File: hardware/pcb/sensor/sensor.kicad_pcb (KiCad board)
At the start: 2 copper layers, 76.2 x 71.1 mm, 14 parts

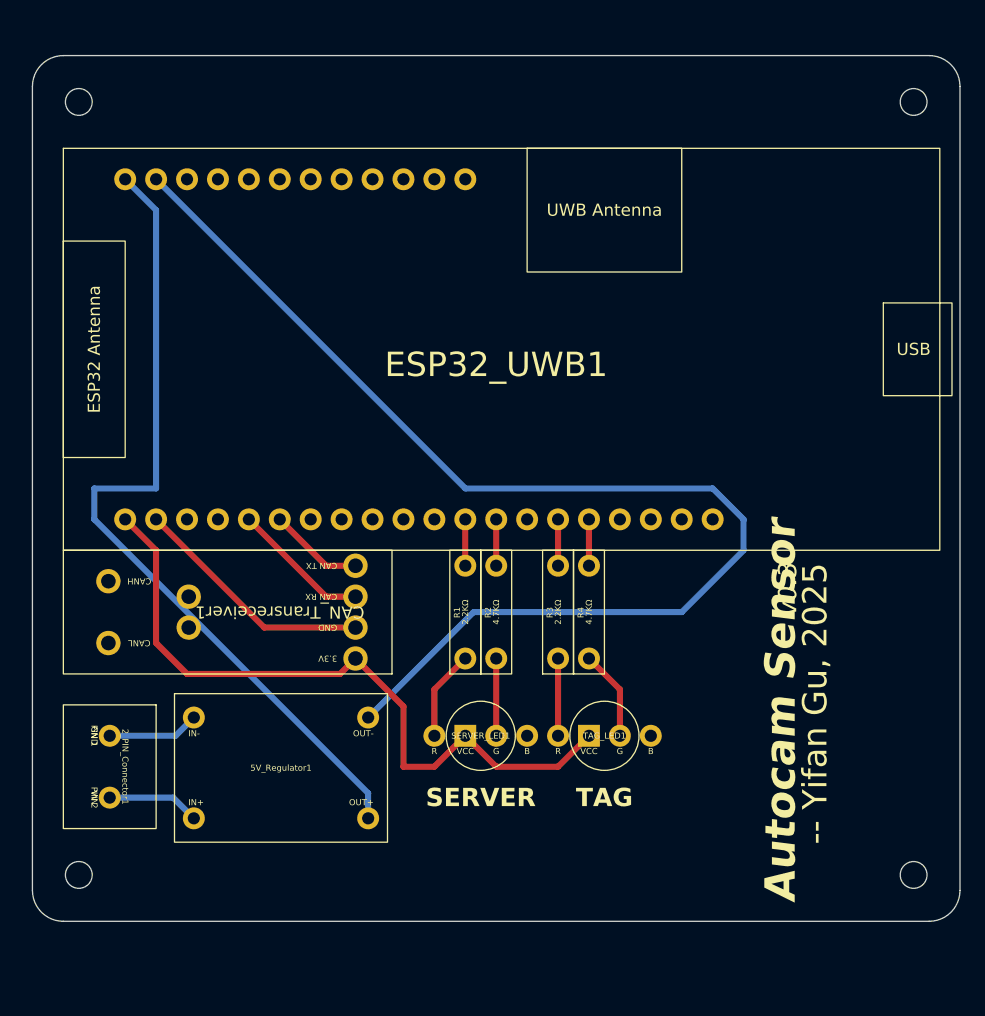
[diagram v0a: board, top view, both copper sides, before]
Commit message: remote: Update PCB for remote.
Fix the issue that GPIO 35 does not have internal PULLUP resistor.
So switch the pin with the gimbal thumbstick input Y, instead of the
drive mode button.

Update sensor and tag pcb as well to reflect the changes.
- tag: Use pin 39 for battery measurement and revert the resistor value
  change that's done in the previous commit.
- sensor: Fix a wiring issue.
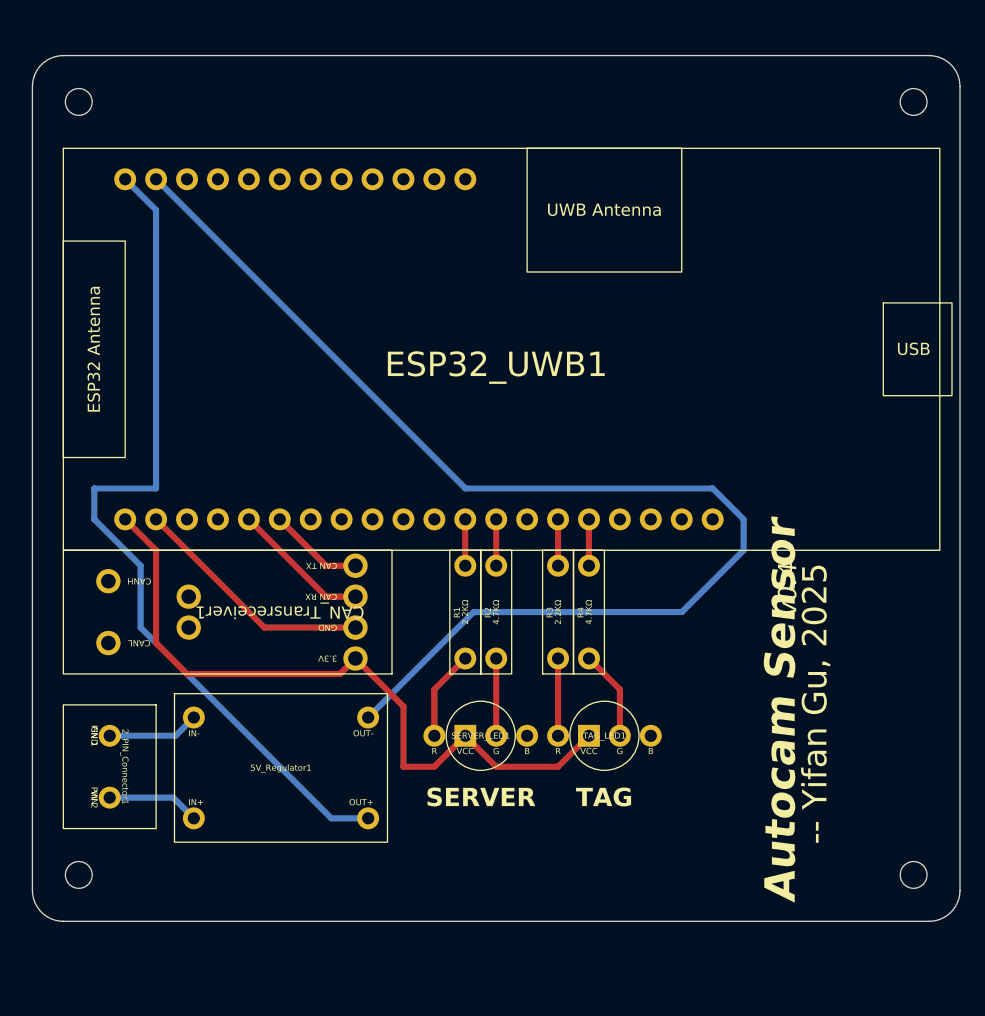
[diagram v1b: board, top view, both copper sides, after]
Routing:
- net Net-(5V_Regulator1-OUT+): track 68.0 -> 69.7 mm
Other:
- board text added: "v0.4"
- board text removed: "v0.3"
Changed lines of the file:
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@@
 	(title_block
 		(title "Autocam Sensor")
-		(date "2025-03-18")
-		(rev "v0.3")
+		(date "2025-03-27")
+		(rev "v0.4")
 	)
 	(layers
@@
 		)
 	)
-	(gr_text "v0.3"
+	(gr_text "v0.4"
 		(at 173.418978 111.513989 90)
 		(layer "F.SilkS")
@@
 			(justify right bottom)
 		)
-		(render_cache "v0.3" 90
+		(render_cache "v0.4" 90
 			(polygon
 				(pts
@@
 			(polygon
 				(pts
-					(xy 171.827481 111.538534) (xy 171.968165 111.691308) (xy 171.968165 112.155217) (xy 171.827481 112.285001)
+					(xy 172.415587 112.363312) (xy 171.849462 112.313669) (xy 171.997382 112.183793) (xy 172.379225 112.216308)
+					(xy 172.469076 112.313669)
 				)
 			)
 			(polygon
 				(pts
-					(xy 173.163978 111.655038) (xy 173.163978 112.401505) (xy 173.023294 112.246899) (xy 173.023294 111.782991)
-				)
-			)
-			(polygon
-				(pts
-					(xy 172.577795 111.576728) (xy 173.134668 111.62637) (xy 172.993893 111.754323) (xy 172.612141 111.721808)
+					(xy 172.577886 111.576728) (xy 173.141996 111.62637) (xy 172.993984 111.754323) (xy 172.612233 111.721808)
 					(xy 172.522565 111.624447)
 				)
@@
 			(polygon
 				(pts
-					(xy 172.379225 111.700833) (xy 171.997657 111.66841) (xy 171.854317 111.513713) (xy 172.415587 111.563355)
+					(xy 172.379225 111.700833) (xy 171.997657 111.66841) (xy 171.849462 111.513713) (xy 172.415587 111.563355)
 					(xy 172.469076 111.618768)
 				)
@@
 	)
 	(segment
-		(start 120.65 82.55)
-		(end 118.11 80.01)
+		(start 119.38 116.84)
+		(end 135.05 132.51)
 		(width 0.5)
 		(layer "B.Cu")
@@
 	)
 	(segment
-		(start 138.07 130.45)
+		(start 115.57 105.41)
 		(end 115.57 107.95)
 		(width 0.5)
@@
 	)
 	(segment
-		(start 120.65 105.41)
-		(end 120.65 82.55)
+		(start 120.65 82.55)
+		(end 120.65 105.41)
 		(width 0.5)
 		(layer "B.Cu")
@@
 	)
 	(segment
-		(start 138.07 132.51)
-		(end 138.07 130.45)
+		(start 118.11 80.01)
+		(end 120.65 82.55)
 		(width 0.5)
 		(layer "B.Cu")
@@
 	)
 	(segment
-		(start 115.57 105.41)
-		(end 120.65 105.41)
+		(start 119.38 111.76)
+		(end 119.38 116.84)
 		(width 0.5)
 		(layer "B.Cu")
@@
 	(segment
 		(start 115.57 107.95)
+		(end 119.38 111.76)
+		(width 0.5)
+		(layer "B.Cu")
+		(net 2)
+	)
+	(segment
+		(start 135.05 132.51)
+		(end 138.07 132.51)
+		(width 0.5)
+		(layer "B.Cu")
+		(net 2)
+	)
+	(segment
+		(start 120.65 105.41)
 		(end 115.57 105.41)
 		(width 0.5)

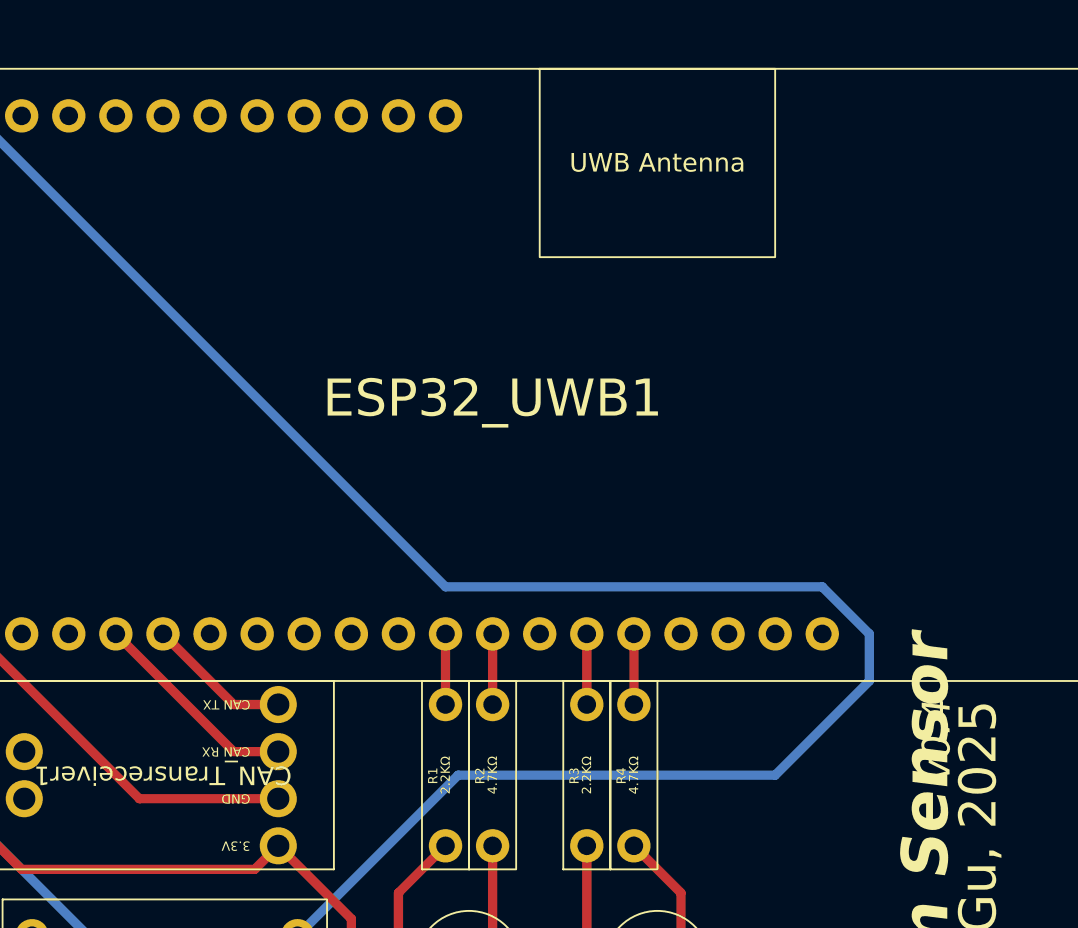
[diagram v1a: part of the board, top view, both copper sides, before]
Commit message: sensor,tag: Update PCB wiring to avoid bootstrap pins.
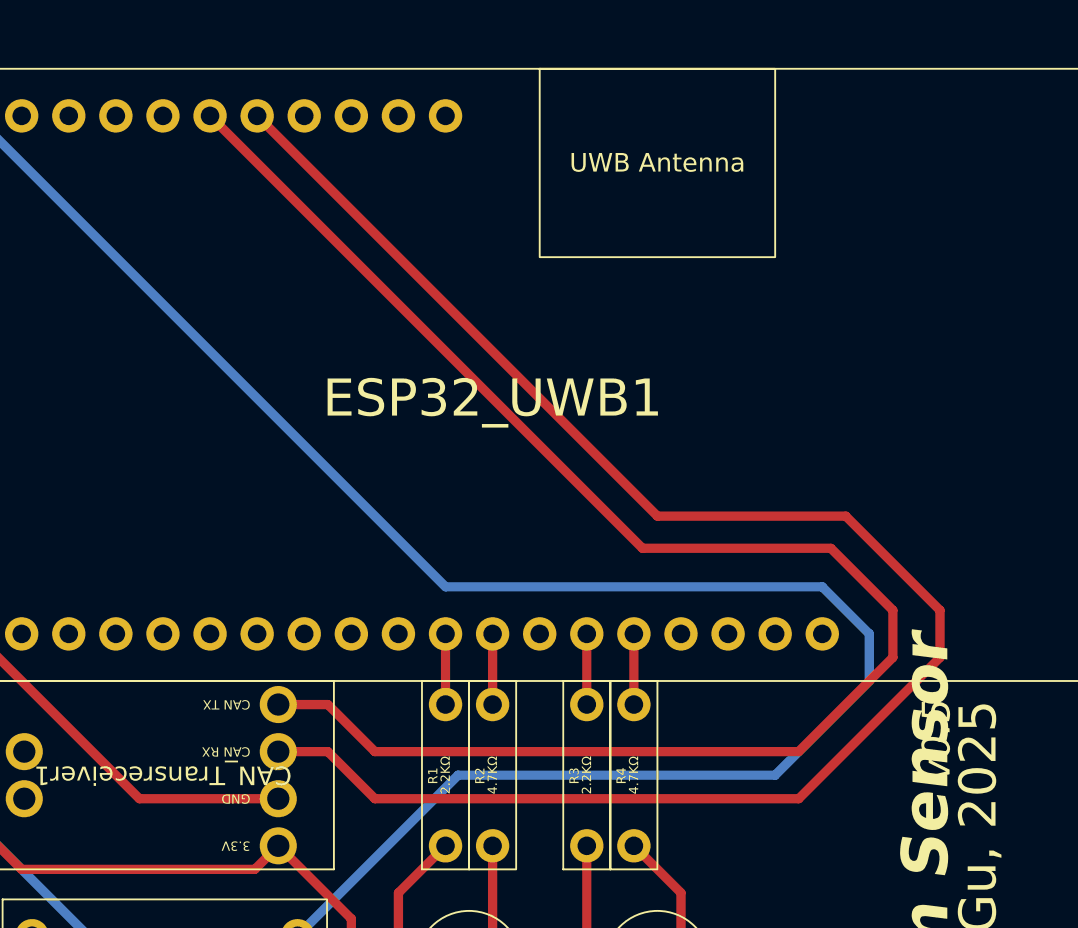
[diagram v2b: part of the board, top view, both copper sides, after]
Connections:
- ESP32_UWB1 pad 27: unconnected-(ESP32_UWB1-IO5-Pad27) -> Net-(CAN_Transreceiver1-CAN_TX)
- ESP32_UWB1 pad 28: unconnected-(ESP32_UWB1-IO16-Pad28) -> Net-(CAN_Transreceiver1-CAN_RX)
- ESP32_UWB1 pad 5: Net-(CAN_Transreceiver1-CAN_RX) -> unconnected-(ESP32_UWB1-IO2-Pad5)
- ESP32_UWB1 pad 6: Net-(CAN_Transreceiver1-CAN_TX) -> unconnected-(ESP32_UWB1-IO12-Pad6)
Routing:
- net Net-(CAN_Transreceiver1-CAN_TX): track 7.93 -> 86.7 mm
- net Net-(CAN_Transreceiver1-CAN_RX): track 11.5 -> 90.3 mm
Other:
- board text added: "v0.5"
- board text removed: "v0.4"

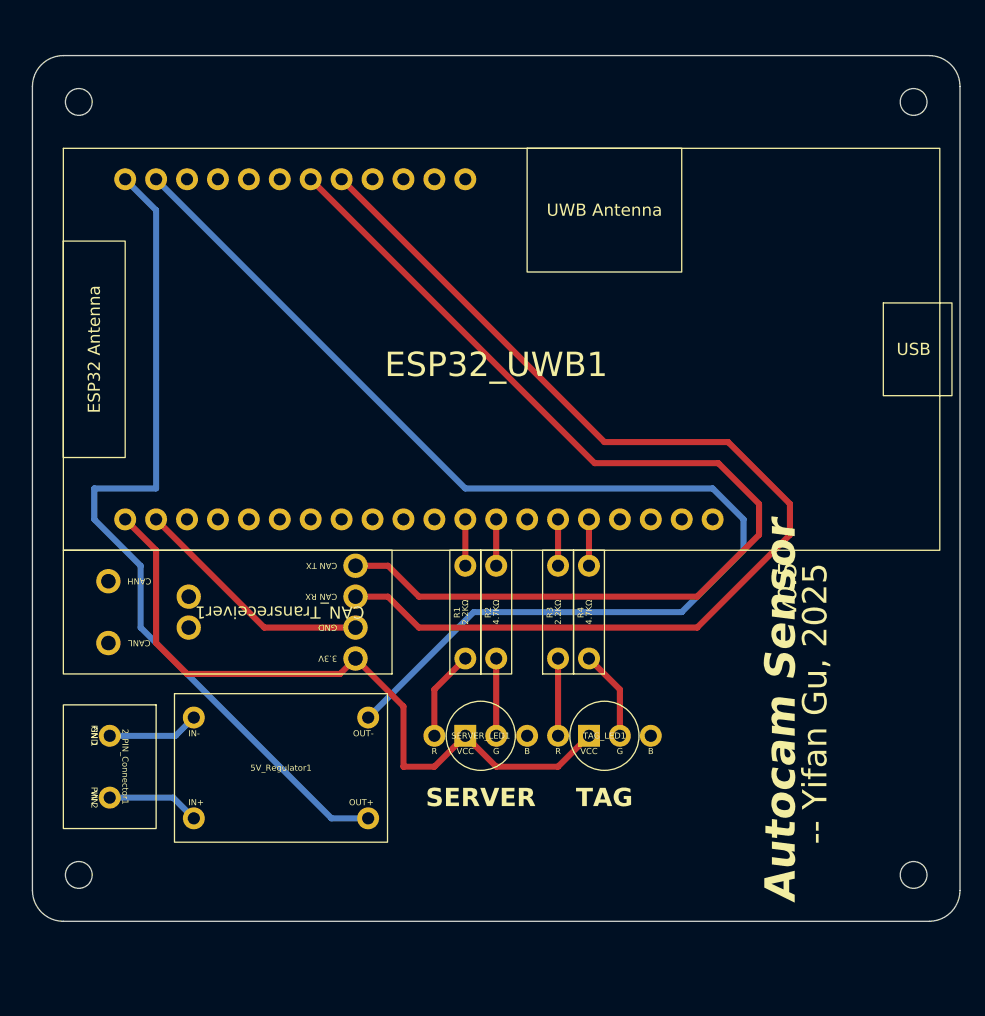
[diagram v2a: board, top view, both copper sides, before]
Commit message: hardware/cad: Finish sensor and server enclosure.
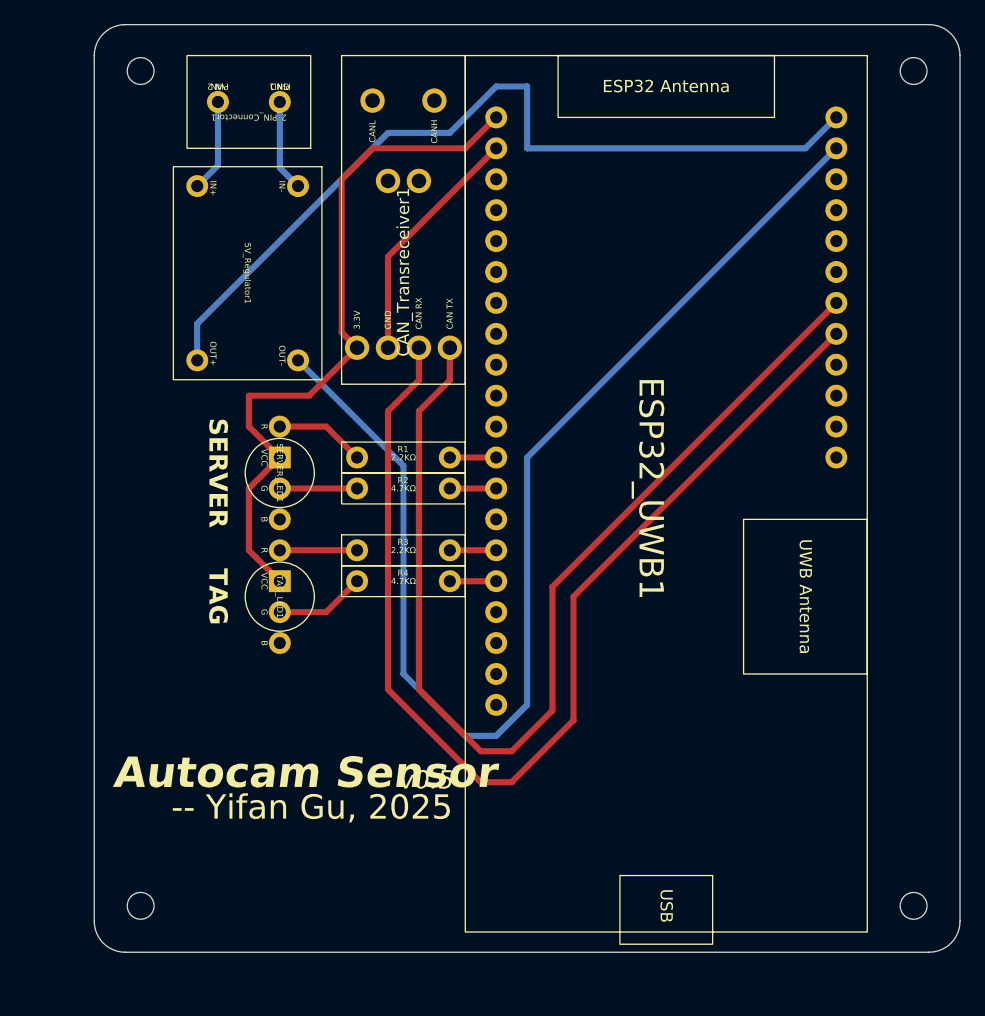
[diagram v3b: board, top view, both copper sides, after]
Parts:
- moved REF** 68.6 mm to (182.9, 71.1), turned to -90 degrees
- moved ESP32_UWB1 66.5 mm to (179.1, 69.8), turned to -90 degrees
- moved REF** 66.2 mm to (119.4, 71.1), turned to -90 degrees
- moved REF** 66.0 mm to (182.9, 139.7), turned to -90 degrees
- moved REF** 63.6 mm to (119.4, 139.7), turned to -90 degrees
- moved 2_PIN_Connector1 57.1 mm to (133.3, 69.8), turned to 180 degrees
- moved CAN_Transreceiver1 52.4 mm to (146.1, 69.8), turned to 90 degrees
- moved 5V_Regulator1 45.0 mm to (134.3, 79.0), turned to -90 degrees
- moved TAG_LED1 29.0 mm to (130.8, 114.3), turned to -90 degrees
- moved SERVER_LED1 27.2 mm to (130.8, 104.1), turned to -90 degrees
- moved R4 20.1 mm to (137.2, 113.0), turned to 0 degrees
- moved R1 18.8 mm to (137.2, 102.9), turned to 0 degrees
- moved R3 18.8 mm to (137.2, 110.5), turned to 0 degrees
- moved R2 18.1 mm to (137.2, 105.4), turned to 0 degrees
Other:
- board size 76.2 x 71.1 mm -> 71.1 x 76.2 mm
